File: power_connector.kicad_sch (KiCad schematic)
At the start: 20 parts, among them U104 XT60PW-F, U104 XT60PW-M

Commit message: feat: component placement, again
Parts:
- C119: footprint Capacitor_SMD:C_0603_1608Metric_Pad1.08x0.95mm_HandSolder -> Capacitor_SMD:C_0805_2012Metric_Pad1.18x1.45mm_HandSolder
- U104: footprint Connector_AMASS:XT60PW-M_1x02_P7.20mm_Horizontal_WP -> Connector_AMASS:XT60PW-F_1x02_P7.20mm_Horizontal
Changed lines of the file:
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@@
       (effects (font (size 1.27 1.27)) (justify left))
     )
-    (property "Footprint" "Capacitor_SMD:C_0603_1608Metric_Pad1.08x0.95mm_HandSolder" (at 170.18 97.79 0)
+    (property "Footprint" "Capacitor_SMD:C_0805_2012Metric_Pad1.18x1.45mm_HandSolder" (at 170.18 97.79 0)
       (effects (font (size 1.27 1.27)) hide)
     )
@@
       (effects (font (size 1.27 1.27)) (justify left))
     )
-    (property "Footprint" "Capacitor_SMD:C_0603_1608Metric_Pad1.08x0.95mm_HandSolder" (at 196.85 97.79 0)
+    (property "Footprint" "Capacitor_SMD:C_0805_2012Metric_Pad1.18x1.45mm_HandSolder" (at 196.85 97.79 0)
       (effects (font (size 1.27 1.27)) hide)
     )
@@
       (effects (font (size 1.27 1.27)) (justify left))
     )
-    (property "Footprint" "Capacitor_SMD:C_0603_1608Metric_Pad1.08x0.95mm_HandSolder" (at 223.52 97.79 0)
+    (property "Footprint" "Capacitor_SMD:C_0805_2012Metric_Pad1.18x1.45mm_HandSolder" (at 223.52 97.79 0)
       (effects (font (size 1.27 1.27)) hide)
     )
@@
       (effects (font (size 1.27 1.27)) (justify left))
     )
-    (property "Footprint" "Capacitor_SMD:C_0603_1608Metric_Pad1.08x0.95mm_HandSolder" (at 236.855 97.79 0)
+    (property "Footprint" "Capacitor_SMD:C_0805_2012Metric_Pad1.18x1.45mm_HandSolder" (at 236.855 97.79 0)
       (effects (font (size 1.27 1.27)) hide)
     )
@@
       (effects (font (size 1.27 1.27)) (justify left))
     )
-    (property "Footprint" "Capacitor_SMD:C_0603_1608Metric_Pad1.08x0.95mm_HandSolder" (at 183.515 120.015 0)
+    (property "Footprint" "Capacitor_SMD:C_0805_2012Metric_Pad1.18x1.45mm_HandSolder" (at 183.515 120.015 0)
       (effects (font (size 1.27 1.27)) hide)
     )
@@
       (effects (font (size 1.27 1.27)) (justify left))
     )
-    (property "Footprint" "Capacitor_SMD:C_0603_1608Metric_Pad1.08x0.95mm_HandSolder" (at 196.85 120.015 0)
+    (property "Footprint" "Capacitor_SMD:C_0805_2012Metric_Pad1.18x1.45mm_HandSolder" (at 196.85 120.015 0)
       (effects (font (size 1.27 1.27)) hide)
     )
@@
       (effects (font (size 1.27 1.27)) (justify left))
     )
-    (property "Footprint" "Capacitor_SMD:C_0603_1608Metric_Pad1.08x0.95mm_HandSolder" (at 170.18 120.015 0)
+    (property "Footprint" "Capacitor_SMD:C_0805_2012Metric_Pad1.18x1.45mm_HandSolder" (at 170.18 120.015 0)
       (effects (font (size 1.27 1.27)) hide)
     )
@@
       (effects (font (size 1.27 1.27)) (justify left))
     )
-    (property "Footprint" "Capacitor_SMD:C_0603_1608Metric_Pad1.08x0.95mm_HandSolder" (at 236.855 120.015 0)
+    (property "Footprint" "Capacitor_SMD:C_0805_2012Metric_Pad1.18x1.45mm_HandSolder" (at 236.855 120.015 0)
       (effects (font (size 1.27 1.27)) hide)
     )
@@
       (effects (font (size 1.27 1.27)) (justify left))
     )
-    (property "Footprint" "Capacitor_SMD:C_0603_1608Metric_Pad1.08x0.95mm_HandSolder" (at 210.185 97.79 0)
+    (property "Footprint" "Capacitor_SMD:C_0805_2012Metric_Pad1.18x1.45mm_HandSolder" (at 210.185 97.79 0)
       (effects (font (size 1.27 1.27)) hide)
     )
@@
       (effects (font (size 1.27 1.27)) (justify left))
     )
-    (property "Footprint" "Connector_AMASS:XT60PW-M_1x02_P7.20mm_Horizontal_WP" (at 58.42 80.01 0)
+    (property "Footprint" "Connector_AMASS:XT60PW-F_1x02_P7.20mm_Horizontal" (at 58.42 80.01 0)
       (effects (font (size 1.27 1.27)) hide)
     )
@@
       (effects (font (size 1.27 1.27)) (justify left))
     )
-    (property "Footprint" "Capacitor_SMD:C_0603_1608Metric_Pad1.08x0.95mm_HandSolder" (at 183.515 97.79 0)
+    (property "Footprint" "Capacitor_SMD:C_0805_2012Metric_Pad1.18x1.45mm_HandSolder" (at 183.515 97.79 0)
       (effects (font (size 1.27 1.27)) hide)
     )
@@
       (effects (font (size 1.27 1.27)) (justify left))
     )
-    (property "Footprint" "Capacitor_SMD:C_0603_1608Metric_Pad1.08x0.95mm_HandSolder" (at 223.52 120.015 0)
+    (property "Footprint" "Capacitor_SMD:C_0805_2012Metric_Pad1.18x1.45mm_HandSolder" (at 223.52 120.015 0)
       (effects (font (size 1.27 1.27)) hide)
     )
@@
       (effects (font (size 1.27 1.27)) (justify left))
     )
-    (property "Footprint" "Capacitor_SMD:C_0603_1608Metric_Pad1.08x0.95mm_HandSolder" (at 210.185 120.015 0)
-      (effects (font (size 1.27 1.27)) hide)
-    )
+    (property "Footprint" "Capacitor_SMD:C_0805_2012Metric_Pad1.18x1.45mm_HandSolder" (at 210.185 120.015 0)
+      (effects (font (size 1.27 1.27)) hide)
+    )

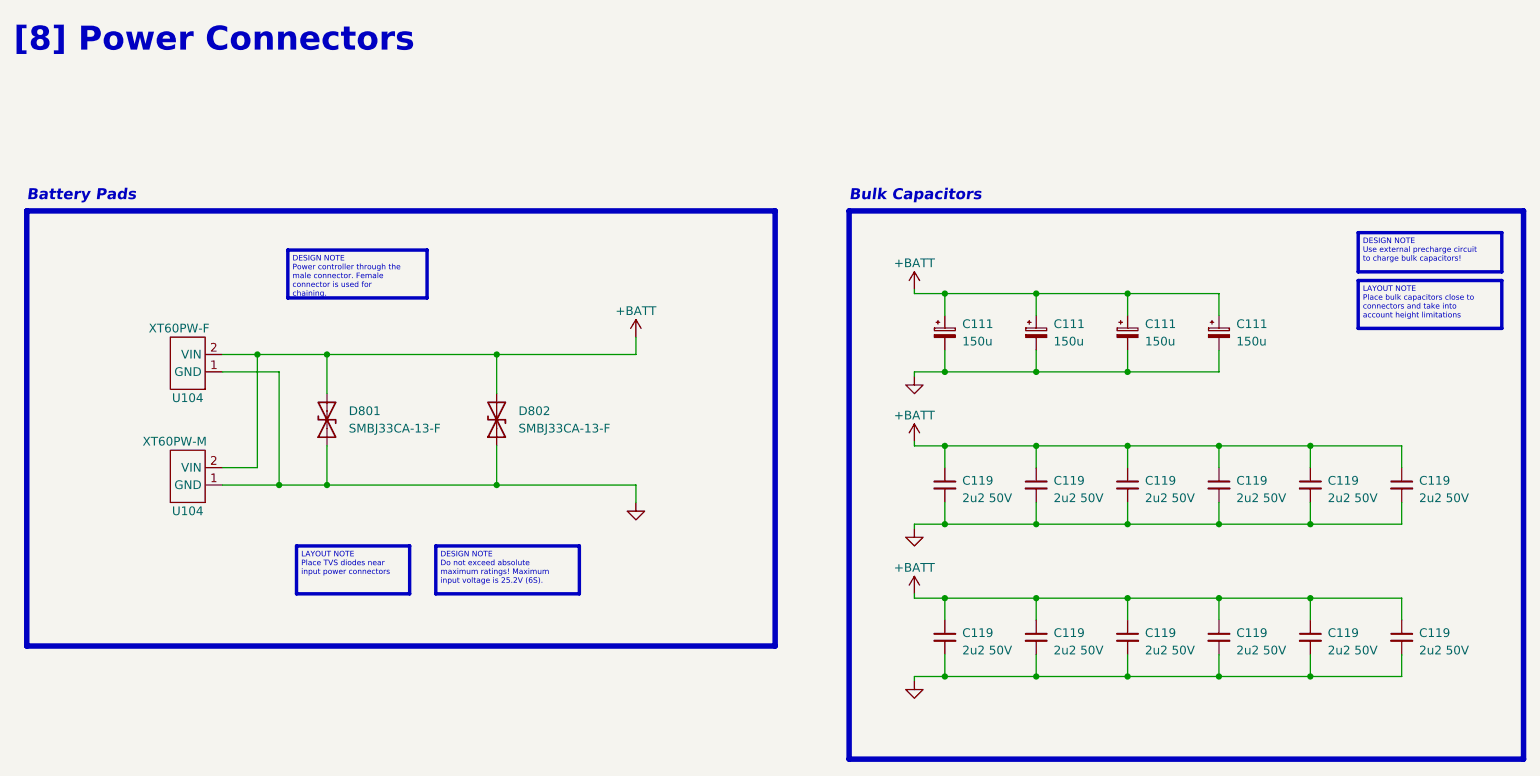
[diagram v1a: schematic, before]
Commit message: feat: finished inverter placement and routing
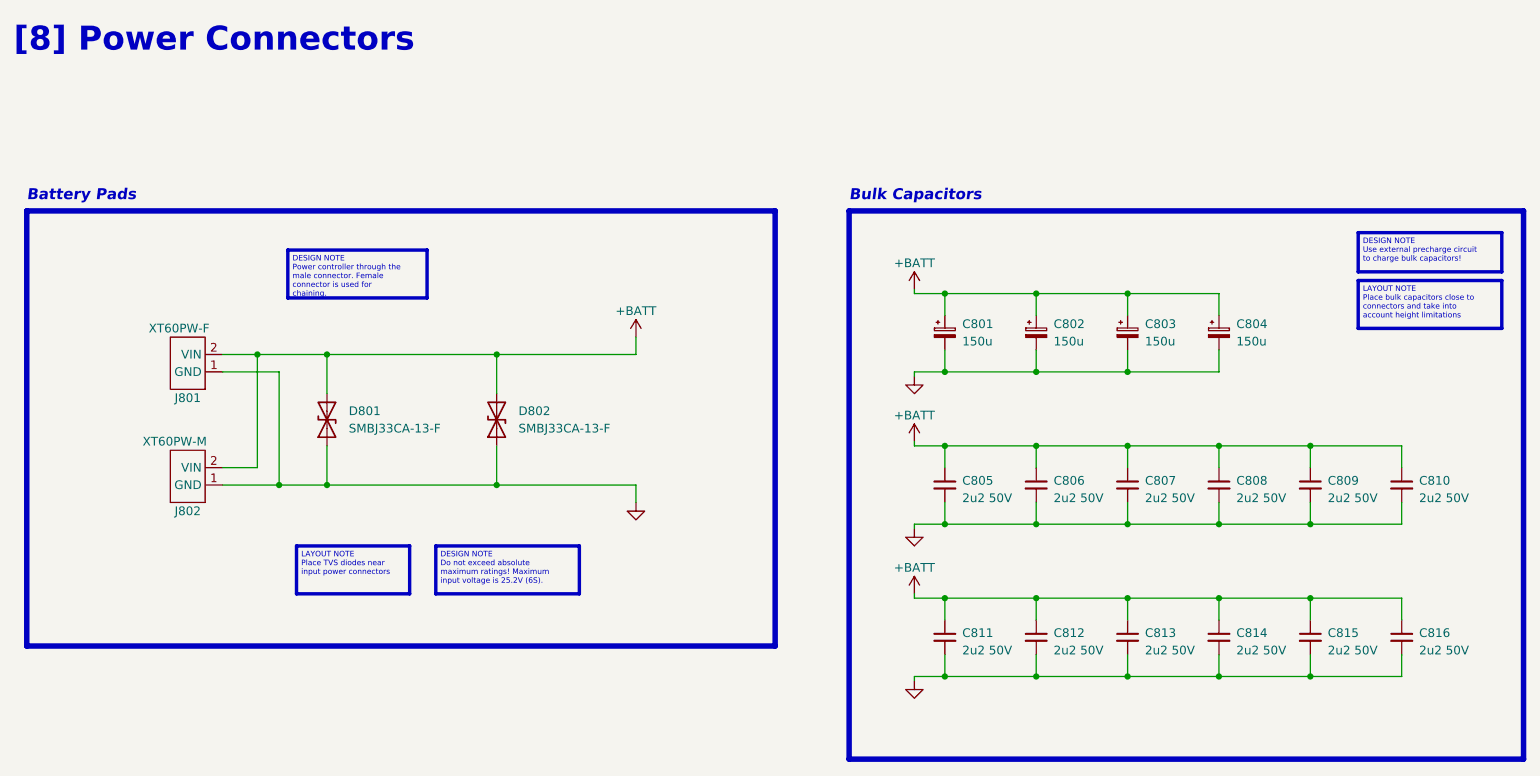
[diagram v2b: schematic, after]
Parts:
- renumbered C111 to C801, C111 to C802, C111 to C803, C111 to C804, C119 to C805, C119 to C806, C119 to C807, C119 to C808, C119 to C809, C119 to C810, C119 to C811, C119 to C812, C119 to C813, C119 to C814, C119 to C815, C119 to C816, U104 to J801, U104 to J802
